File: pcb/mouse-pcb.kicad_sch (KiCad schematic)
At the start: 0 parts

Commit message: feat: gitignore, and pmw3395 added
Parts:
- added U1: PAW3395-T6QU, paw3395:paw3395, symbol Mouse_sensor:PAW3395-T6QU

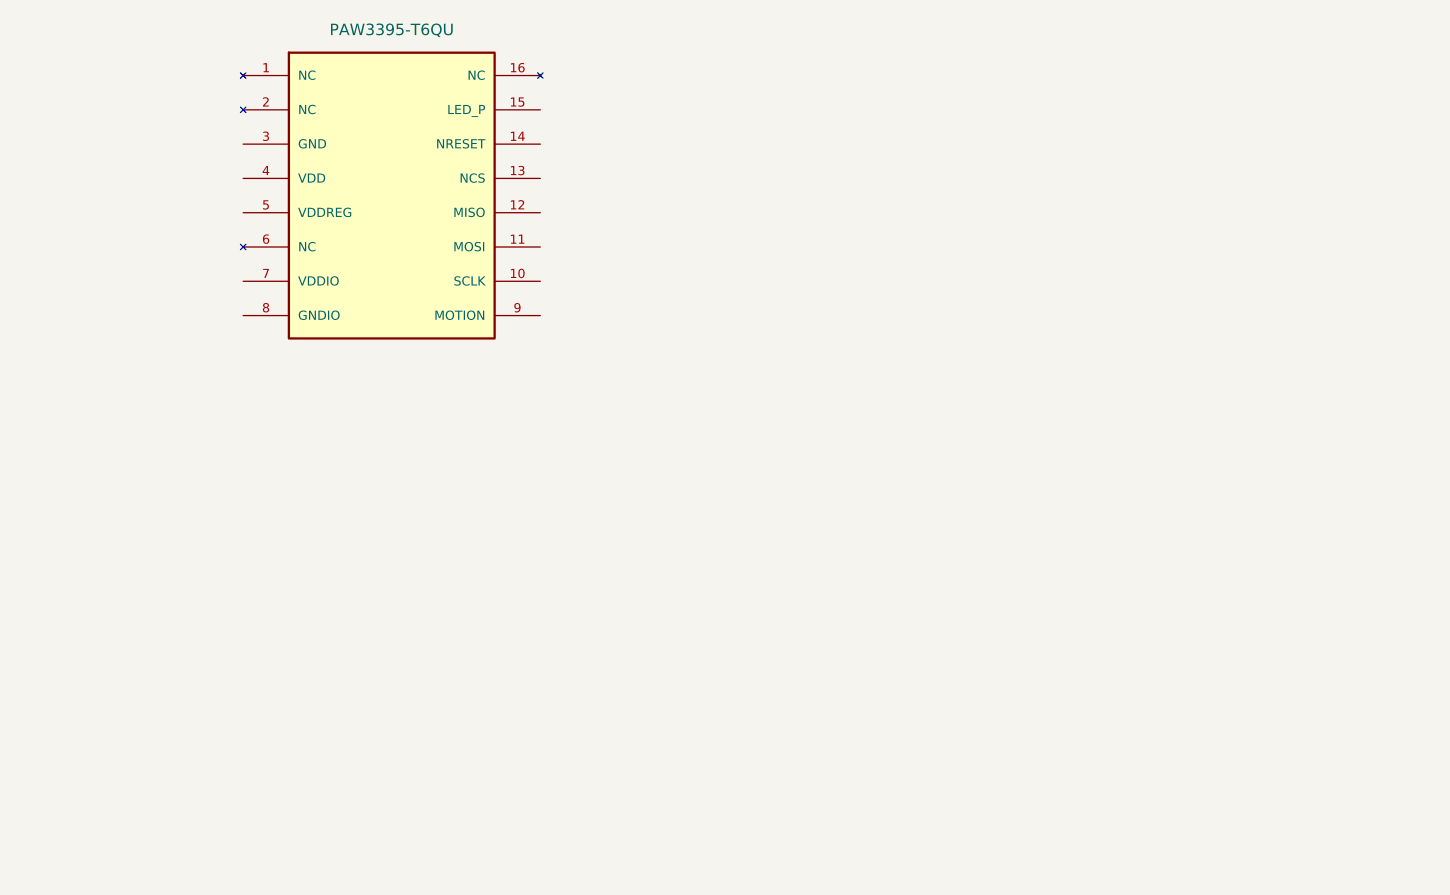
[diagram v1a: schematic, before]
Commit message: feat: add new library for the mouse
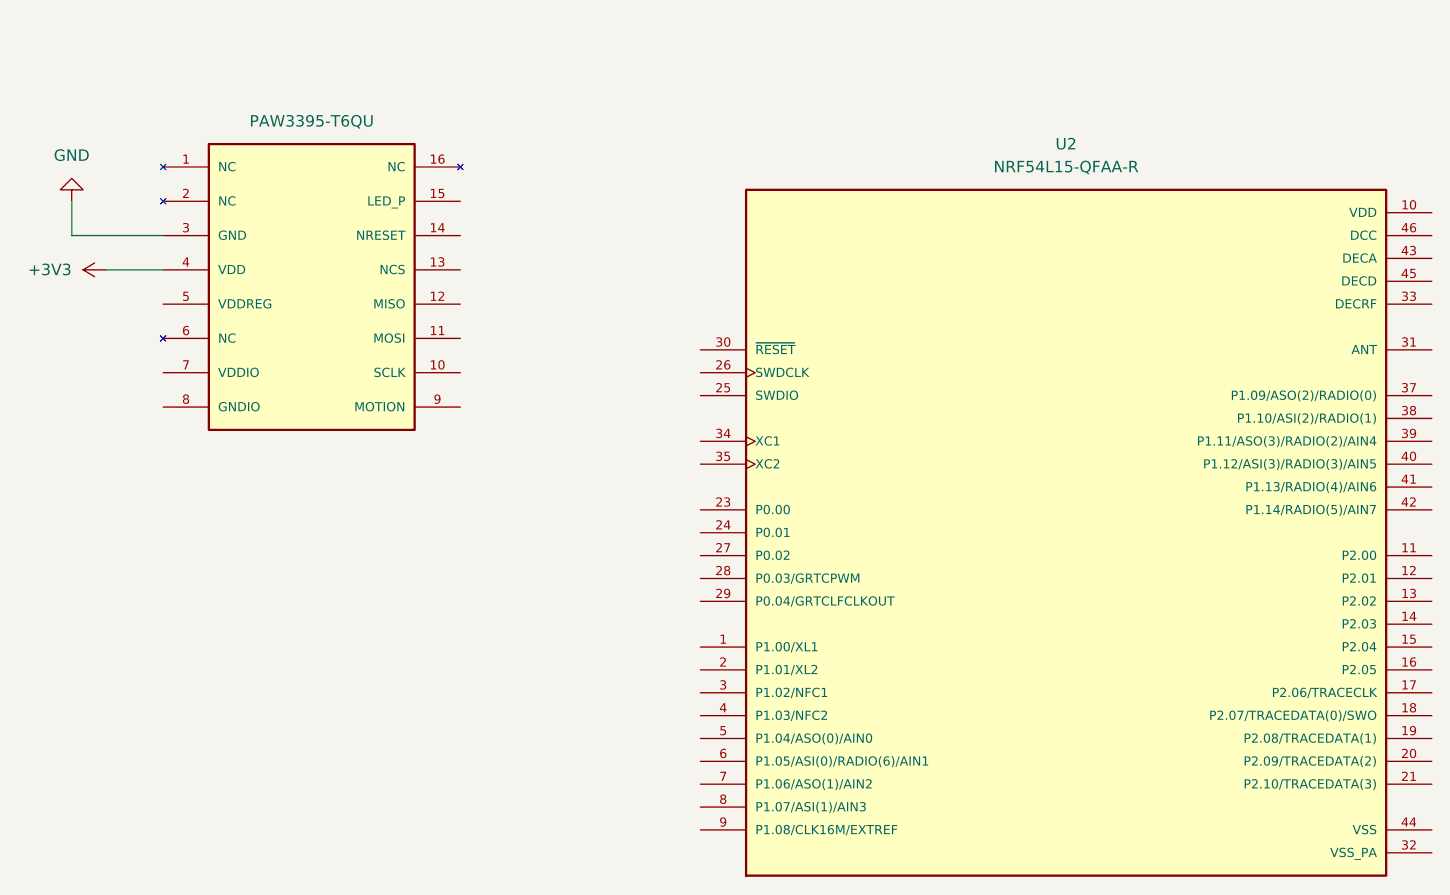
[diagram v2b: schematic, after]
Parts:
- removed U1: PAW3395-T6QU, paw3395:paw3395, symbol Mouse_sensor:PAW3395-T6QU
- added U1: PAW3395-T6QU, mouse_library:paw3395, symbol mouse_library:PAW3395-T6QU
- added U2: NRF54L15-QFAA-R, mouse_library:QFN40P600X600X90-49N, symbol mouse_library:NRF54L15-QFAA-R
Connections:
- new net +3V3: U1.4 (VDD)
- new net GND: U1.3 (GND)
- new net VDD: U2.10 (VDD), U2.22 (VDD), U2.36 (VDD), U2.47 (VDD), U2.48 (VDD)
- new net VSS: U2.44 (VSS), U2.49 (VSS)

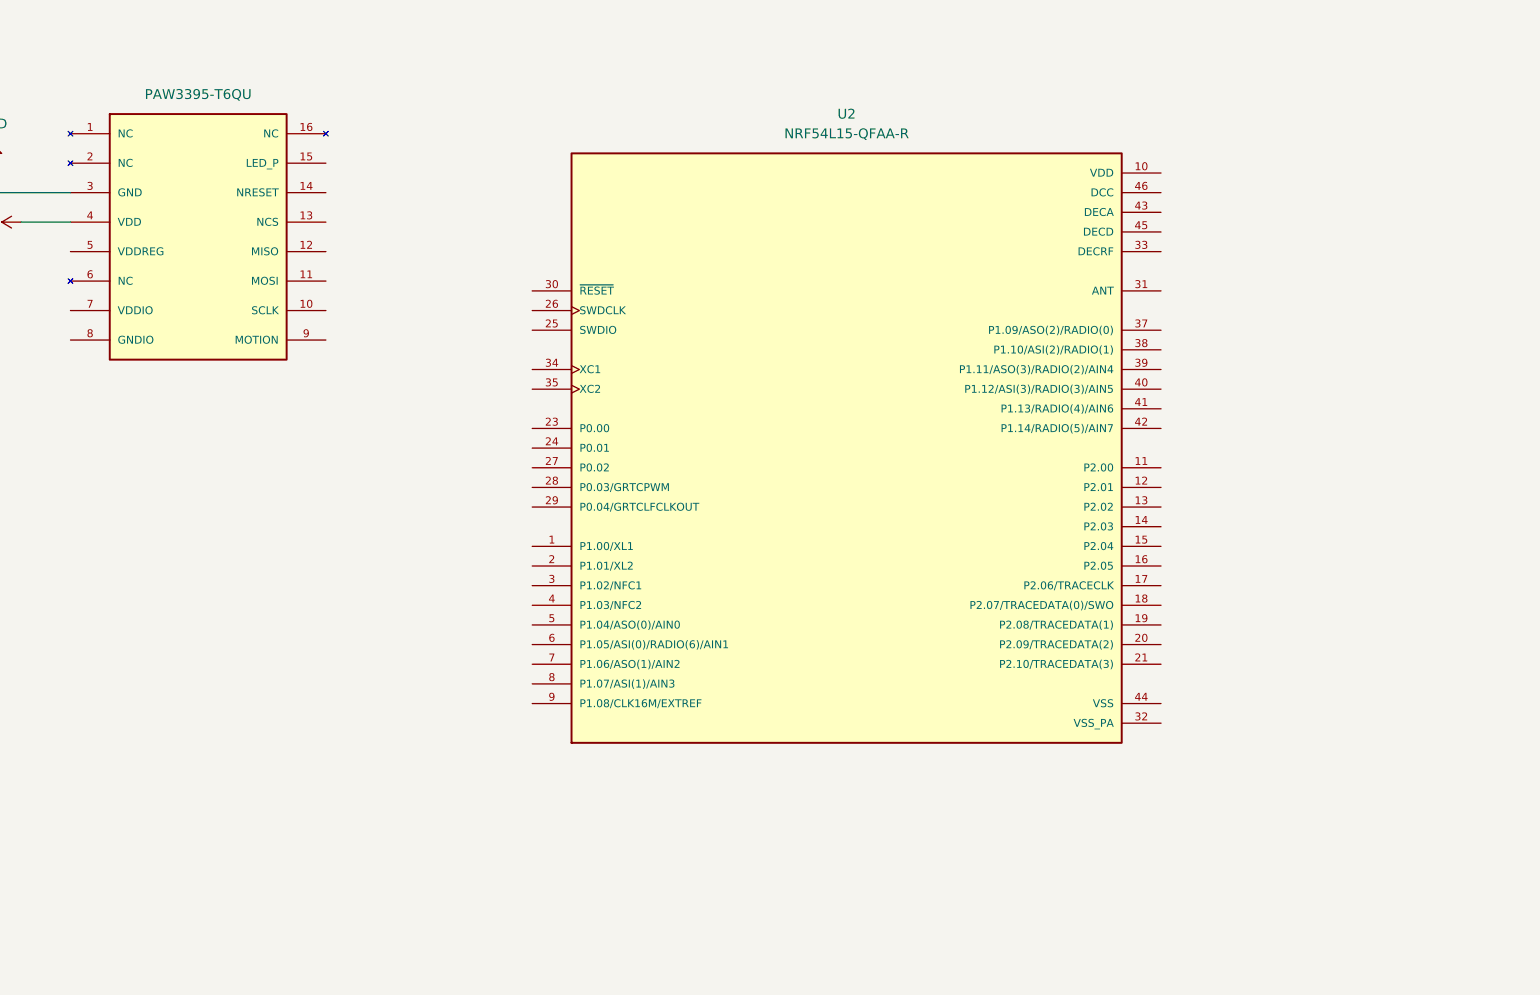
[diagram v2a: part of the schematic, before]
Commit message: feat: add more components to the library
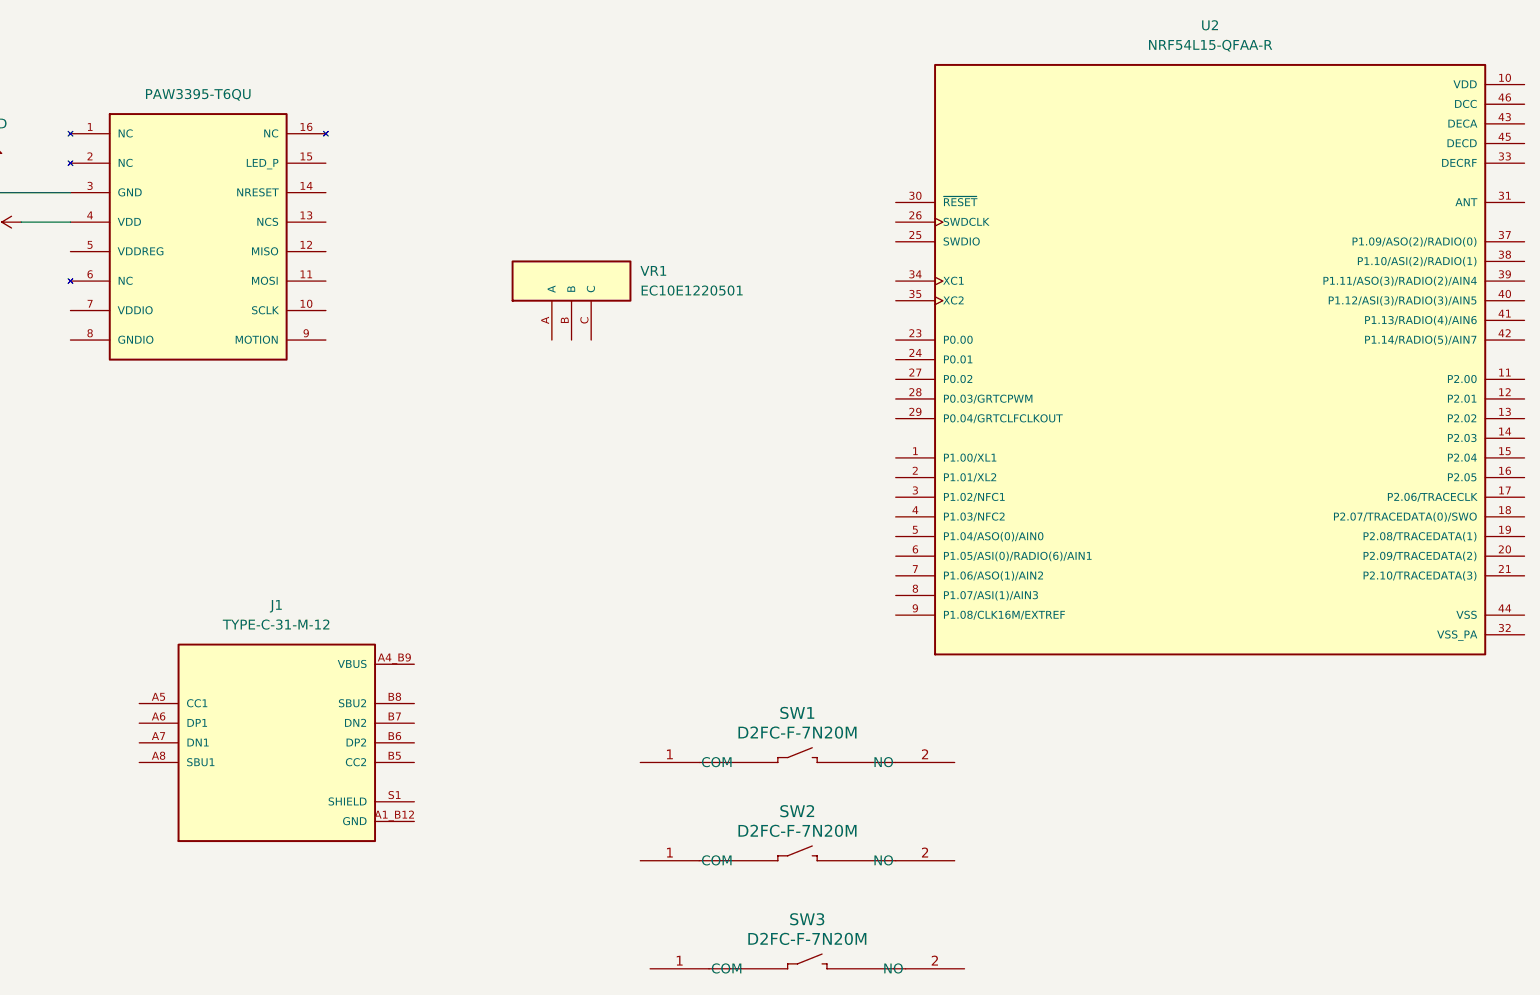
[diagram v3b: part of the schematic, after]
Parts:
- added J1: TYPE-C-31-M-12, mouse_library:HRO_TYPE-C-31-M-12, symbol mouse_library:TYPE-C-31-M-12
- added SW1, SW2, SW3: D2FC-F-7N20M, mouse_library:SW_D2FC_OMR, symbol mouse_library:D2FC-F-7N20M
- added VR1: EC10E1220501, mouse_library:TRIM_EC10E1220501, symbol mouse_library:EC10E1220501
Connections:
- net GND: now also J1.A1_B12 (GND), J1.B1_A12 (GND)
- new net: J1.S1 (SHIELD), J1.S2 (SHIELD), J1.S3 (SHIELD), J1.S4 (SHIELD)
- new net VBUS: J1.A4_B9 (VBUS), J1.B4_A9 (VBUS)
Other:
- moved on the sheet: U2

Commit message: feat: adding all the passive for mouse
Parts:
- added C1: 4.7uF, Capacitor_SMD:C_0805_2012Metric_Pad1.18x1.45mm_HandSolder, symbol Device:C
- added C2, C4, C5: 100nF, Capacitor_SMD:C_0805_2012Metric_Pad1.18x1.45mm_HandSolder, symbol Device:C
- added C3, C6: 10uF, Capacitor_SMD:C_0805_2012Metric_Pad1.18x1.45mm_HandSolder, symbol Device:C
- added C7: 33uF, Capacitor_SMD:C_0805_2012Metric_Pad1.18x1.45mm_HandSolder, symbol Device:C
- added R1: 10K, Resistor_SMD:R_0805_2012Metric_Pad1.20x1.40mm_HandSolder, symbol Device:R_US
- added R2: 5R6, Resistor_SMD:R_0805_2012Metric_Pad1.20x1.40mm_HandSolder, symbol Device:R_US
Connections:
- net +3V3: now also U1.7 (VDDIO), C3.1, C4.1, R1.1; no longer U1.4 (VDD)
- net GND: now also U1.8 (GNDIO), C1.2, C2.2, C3.2, C4.2, C5.2, C6.2, C7.2
- net SCLK: now reaches U1.10 (SCLK)
- net MOSI: now reaches U1.11 (MOSI)
- net MISO: now reaches U1.12 (MISO)
- net MISO: now also R1.2
- net NCS: now reaches U1.13 (NCS)
- net NRESET: now reaches U1.14 (NRESET)
- net at U1.15 (LED_P): now also R2.1
- net VDDREG: now reaches U1.5 (VDDREG)
- net VDDREG: now also C1.1, C2.1
- net MOTION: now reaches U1.9 (MOTION)
- new net +1V9: C5.1, C6.1, C7.1, R2.2, U1.4 (VDD)
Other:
- note added: "Mouse Sensor"
- moved on the sheet: J1, VR1

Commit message: feat: common circuits for chip, antenna remaining
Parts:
- added C10: 10uF, Capacitor_SMD:C_0402_1005Metric_Pad0.74x0.62mm_HandSolder, symbol Device:C
- added C11, C12, C8, C9: 100nF, Capacitor_SMD:C_0201_0603Metric_Pad0.64x0.40mm_HandSolder, symbol Device:C
- added C13, C14: 2.2uf, Capacitor_SMD:C_0201_0603Metric_Pad0.64x0.40mm_HandSolder, symbol Device:C
- added C15: 2.2nf, Capacitor_SMD:C_0201_0603Metric_Pad0.64x0.40mm_HandSolder, symbol Device:C
- added C16: 10nf, Capacitor_SMD:C_0201_0603Metric_Pad0.64x0.40mm_HandSolder, symbol Device:C
- added FB1: FerriteBead, Inductor_SMD:L_0201_0603Metric_Pad0.64x0.40mm_HandSolder, symbol Device:FerriteBead
- added L1: 4.7uH, Inductor_SMD:L_0603_1608Metric_Pad1.05x0.95mm_HandSolder, symbol Device:L
- added Y1: Crystal_GND24, Crystal:Crystal_SMD_2016-4Pin_2.0x1.6mm, symbol Device:Crystal_GND24
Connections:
- net VDD is gone; now on net +3V3: U2.10 (VDD), U2.22 (VDD), U2.36 (VDD), U2.47 (VDD), U2.48 (VDD)
- net VSS is gone; now on net GND: U2.44 (VSS), U2.49 (VSS)
- net +3V3: now also C10.1, C11.1, C12.1, C8.1, C9.1
- net GND: now also U2.32 (VSS_PA), C10.2, C11.2, C12.2, C13.2, C14.2, C15.2, C16.2, C8.2, C9.2, Y1.2 (G), Y1.4 (G)
- net SWDIO: now reaches U2.25 (SWDIO)
- net SWDCLK: now reaches U2.26 (SWDCLK)
- net RESET: now reaches U2.30 (~{RESET})
- net DECA: now reaches U2.33 (DECRF)
- net DECA: now also U2.43 (DECA), C13.1, C15.1, C16.1, FB1.2
- net at U2.34 (XC1): now also Y1.1
- net at U2.35 (XC2): now also Y1.3
- net DECD: now reaches U2.45 (DECD)
- net DECD: now also C14.1, FB1.1, L1.2
- net DCC: now reaches U2.46 (DCC)
- net DCC: now also L1.1
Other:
- moved on the sheet: J1, SW1, SW2, SW3, U2, VR1

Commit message: feat: new micro, and antenna
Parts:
- removed C10: 10uF, Capacitor_SMD:C_0402_1005Metric_Pad0.74x0.62mm_HandSolder, symbol Device:C
- removed C11, C12, C8, C9: 100nF, Capacitor_SMD:C_0201_0603Metric_Pad0.64x0.40mm_HandSolder, symbol Device:C
- removed C13, C14: 2.2uf, Capacitor_SMD:C_0201_0603Metric_Pad0.64x0.40mm_HandSolder, symbol Device:C
- removed C15: 2.2nf, Capacitor_SMD:C_0201_0603Metric_Pad0.64x0.40mm_HandSolder, symbol Device:C
- removed C16: 10nf, Capacitor_SMD:C_0201_0603Metric_Pad0.64x0.40mm_HandSolder, symbol Device:C
- removed FB1: FerriteBead, Inductor_SMD:L_0201_0603Metric_Pad0.64x0.40mm_HandSolder, symbol Device:FerriteBead
- removed U2: NRF54L15-QFAA-R, mouse_library:QFN40P600X600X90-49N, symbol mouse_library:NRF54L15-QFAA-R
- removed Y1: Crystal_GND24, Crystal:Crystal_SMD_2016-4Pin_2.0x1.6mm, symbol Device:Crystal_GND24
- added ANT1: ANT016008LCS2442MA2, mouse_library:ANT_ANT016008LCS2442MA2, symbol mouse_library:ANT016008LCS2442MA2
- added L2: 3nH, Inductor_SMD:L_0201_0603Metric, symbol Device:L
- added U2: NRF52840-QIAA-R7, mouse_library:NORDIC_NRF52840-QIAA-R7, symbol mouse_library:NRF52840-QIAA-R7
- C1, C2, C3, C4, C5, C6, C7: footprint Capacitor_SMD:C_0805_2012Metric_Pad1.18x1.45mm_HandSolder -> Capacitor_SMD:C_0805_2012Metric
- L1: value 4.7uH -> 2nH; footprint Inductor_SMD:L_0603_1608Metric_Pad1.05x0.95mm_HandSolder -> Inductor_SMD:L_0201_0603Metric; LCSC_PART_NUMBER C114862 -> C86125; MPN LQM18PN4R7MFRL -> LQP03TN2N0B02D
- R1: footprint Resistor_SMD:R_0805_2012Metric_Pad1.20x1.40mm_HandSolder -> Resistor_SMD:R_0805_2012Metric
- R2: value 5R6 -> 6R8; footprint Resistor_SMD:R_0805_2012Metric_Pad1.20x1.40mm_HandSolder -> Resistor_SMD:R_0805_2012Metric; LCSC_PART_NUMBER C2889457 -> C2889463; MPN 0805 ±1% 5Ω6 -> 0805 ±1% 6Ω8
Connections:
- net GND: now also L2.1
- net +1V9 renamed +2V
- net DCC renamed ANT
- net ANT: now also L2.2
- net DECD: no longer names the net of L1.2
- net DECD: now also ANT1.4 (FEEDING)
- new net RAD: ANT1.1 (RADIATOR_ELECTRODE)
- new net VDD: U2.A22 (VDD), U2.AD14 (VDD), U2.AD23 (VDD), U2.B1 (VDD), U2.W1 (VDD)
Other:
- note added: "Antenna"
- note added: "Battery Management IC — TI BQ25180"
- note added: "C209892"
- note added: "LDO 1.9V - Microchip MCP1812A (set to 1.8V or 2.0V)"
- note added: "LDO 3.3V - ST STLQ020C33R"
- note added: "NRF_POWER->DCDCEN = 1 TODO ON FIRMWARE"
- note added: "USBLC6-2SC6"
- note added: "circuits mcu"
